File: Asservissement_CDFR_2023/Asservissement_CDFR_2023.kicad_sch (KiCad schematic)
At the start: 21 parts

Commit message: add one driver a3930
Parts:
- added C10, C11, C12: 47nF, symbol Device:C_Small
- added C13, C9: 1uF, symbol Device:C
- added C14: 220uF, symbol Device:C_Polarized
- added C7: 100nf, symbol Device:C
- added C8: 470nF, symbol Device:C
- added CT1: 470pF, symbol Device:C
- added IC1: A3930KJPTR-T, A3930KJPTR-T:A3930KJPTRT, symbol A3930:A3930KJPTR-T
- added J4: Conn_01x05, symbol Connector_Generic:Conn_01x05
- added J5: Conn_01x03, symbol Connector_Generic:Conn_01x03
- added Q1, Q2, Q3, Q4, Q5, Q6: QM6006D, Package_TO_SOT_SMD:TO-252-2, symbol Transistor_FET:QM6006D
- added R10: 0.056, symbol Device:R
- added R11, R12, R13, R14, R8, R9: 560, symbol Device:R
- added R4, RT1: 56k, symbol Device:R
- added R5: 100k, symbol Device:R
- added R6, R7: R, symbol Device:R
- gave numbers to parts that had none: 21
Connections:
- net +5V: now also J4.5 (Pin_5), R5.2, R6.1
- net +BATT: now also C13.1, C14.1, C7.1, IC1.24 (VDRAIN_), IC1.45 (VBB), Q1.2 (D), Q3.2 (D), Q5.2 (D)
- net -BATT renamed GND
- net GND: now also C13.2, C14.2, C7.2, C9.1, CT1.2, IC1.17 (TEST_), IC1.21 (CSN_), IC1.41 (AGND_1), IC1.49 (AGND_2), J4.1 (Pin_1), R10.2, R4.2, R7.2, RT1.2
- new net: IC1.20 (REF_), R5.1
- new net: IC1.29 (GHB), R12.1
- new net: Q4.1 (G), R12.2
- new net: Q3.1 (G), R11.2
- new net: C11.2, IC1.28 (SB), J5.2 (Pin_2), Q3.3 (S), Q4.2 (D)
- new net: Q5.1 (G), R13.2
- new net: C10.2, IC1.31 (SA), J5.3 (Pin_3), Q5.3 (S), Q6.2 (D)
- new net: CT1.1, IC1.16 (RC_), RT1.1
- new net: IC1.36 (GLA), R13.1
- new net: C11.1, IC1.30 (CB)
- new net: IC1.10 (H1_), J4.4 (Pin_4)
- new net: IC1.11 (H2_), J4.3 (Pin_3)
- new net: IC1.12 (H3_), J4.2 (Pin_2)
- new net: IC1.18 (RDEAD_), R4.1
- new net: IC1.22 (CSP_), IC1.38 (LSS), Q2.3 (S), Q4.3 (S), Q6.3 (S), R10.1
- new net: IC1.23 (VDSTH_), R6.2, R7.1
- new net: C12.2, IC1.25 (SC), J5.1 (Pin_1), Q1.3 (S), Q2.2 (D)
- new net: IC1.26 (GHC), R9.1
- new net: C12.1, IC1.27 (CC)
- new net: IC1.32 (GHA), R14.1
- new net: C10.1, IC1.33 (CA)
- new net: IC1.34 (GLC), R8.1
- new net: IC1.35 (GLB), R11.1
- new net: C9.2, IC1.40 (VREG)
- new net: C8.2, IC1.42 (CP1)
- new net: C8.1, IC1.43 (CP2)
- new net: Q1.1 (G), R8.2
- new net: Q6.1 (G), R14.2
- new net: Q2.1 (G), R9.2
- new net MODE_1: IC1.15 (MODE_)
- new net action_fault: IC1.39 (ESF)
- new net dir_info_1: IC1.44 (DIRO)
- new net direction_controle_1: IC1.9 (DIR_)
- new net disable_1: IC1.46 (COAST)
- new net erreur_1_1: IC1.5 (FF2_)
- new net erreur_2_1: IC1.6 (FF1_)
- new net frein_1: IC1.8 (BRAKE_)
- new net reset_1: IC1.2 (RESET_)
- new net speed_controle_1: IC1.14 (PWM_)
- new net vitesse_1: IC1.7 (TACHO_)
- no-connect marks 0 -> 8
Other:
- note added: "Blank time 650ns"
- note added: "CBOOT = QGATE × 20 / VBOOT Vboot = Vreg"
- note added: "Cesf 20 times larger than the bootstrap capacitor"
- note added: "ID max = 35A => Vds = 0.5V VDSTH = 0.5V"
- note added: "ITRIP = (VREF - VOOS) / (RSENSE×AV) Av = 19 Voos = 0.32V Vref = 4V max (limité) Itrip = courant max"
- note added: "Piste indépendant faible impédance pour lss"
- note added: "Vdrain : close to the drain connections of the high-side FETs, with an independent trace"
- note added: "tBLANK (µs) = 1260× CT (µF) fOSC ≈ 1/(RTCT + tBLANK + tDEAD) fOSC < fPWM"
- moved on the sheet: J1

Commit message: driver set up
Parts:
- removed IC1: A3930KJPTR-T, A3930KJPTR-T:A3930KJPTRT, symbol A3930:A3930KJPTR-T
- removed U1, U2: LM317_TO-263, Package_TO_SOT_SMD:TO-263-2, symbol Regulator_Linear:LM317_TO-263
- added C? (x3): 47nF, Capacitor_SMD:C_0805_2012Metric_Pad1.18x1.45mm_HandSolder, symbol Device:C_Small
- added C?: 100nF, Capacitor_SMD:C_0805_2012Metric_Pad1.18x1.45mm_HandSolder, symbol Device:C
- added C? (x2): 10uF, Capacitor_SMD:C_0805_2012Metric_Pad1.18x1.45mm_HandSolder, symbol Device:C
- added C? (x2): 1uF, Capacitor_SMD:C_0805_2012Metric_Pad1.18x1.45mm_HandSolder, symbol Device:C
- added C?: 220uF, symbol Device:C_Polarized
- added C?: 470nF, Capacitor_SMD:C_0805_2012Metric_Pad1.18x1.45mm_HandSolder, symbol Device:C
- added CT?: 470pF, Capacitor_SMD:C_0805_2012Metric_Pad1.18x1.45mm_HandSolder, symbol Device:C
- added IC? (x2): A3930KJPTR-T, A3930KJPTR-T:A3930KJPTRT, symbol a3930kjptr-t:A3930KJPTR-T
- added J?: Conn_01x05, symbol Connector_Generic:Conn_01x05
- added J? (x3): Conn_01x03, symbol Connector_Generic:Conn_01x03
- added JP?: Jumper_3_Open, symbol Jumper:Jumper_3_Open
- added Q? (x6): QM6006D, Package_TO_SOT_SMD:TO-252-2, symbol Transistor_FET:QM6006D
- added R15, R16, R17, R? (x5): R, Resistor_SMD:R_0805_2012Metric_Pad1.20x1.40mm_HandSolder, symbol Device:R
- added R? (x6): 560, Resistor_SMD:R_0805_2012Metric_Pad1.20x1.40mm_HandSolder, symbol Device:R
- added R?: 0.018, Resistor_SMD:R_2512_6332Metric, symbol Device:R
- added R?, RT?: 56k, Resistor_SMD:R_0805_2012Metric_Pad1.20x1.40mm_HandSolder, symbol Device:R
- added R?: 10k, symbol Device:R
- added R?: 100k, Resistor_SMD:R_0805_2012Metric_Pad1.20x1.40mm_HandSolder, symbol Device:R
- added U1, U2: LM317_SOT-223, Package_TO_SOT_SMD:SOT-223-3_TabPin2, symbol Regulator_Linear:LM317_SOT-223
- C10, C11, C12, C13, C8, C9, CT1: footprint (none) -> Capacitor_SMD:C_0805_2012Metric_Pad1.18x1.45mm_HandSolder
- C7: value 100nf -> 100nF; footprint (none) -> Capacitor_SMD:C_0805_2012Metric_Pad1.18x1.45mm_HandSolder
- R10: value 0.056 -> 0.018; footprint (none) -> Resistor_SMD:R_2512_6332Metric; Imax pour 3.4A max -> pour 10.7A max
- R11, R12, R13, R14, R4, R5, R6, R7, R8, R9, RT1: footprint (none) -> Resistor_SMD:R_0805_2012Metric_Pad1.20x1.40mm_HandSolder
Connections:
- net +3.3V: now also JP?.3 (B), U2.2 (VO)
- net +5V: now also J?.5 (Pin_5), R15.1, R16.1, R17.1, R?.1, R?.1, R?.1, R?.1, R?.2, U1.2 (VO)
- net +BATT: now also C?.1, C?.1, C?.1, C?.1, C?.1, IC?.24 (VDRAIN_), IC?.24 (VDRAIN_), IC?.45 (VBB), IC?.45 (VBB), Q?.2 (D), Q?.2 (D), Q?.2 (D)
- net GND: now also C?.1, C?.2, C?.2, C?.2, C?.2, C?.2, CT?.2, IC?.17 (TEST_), IC?.17 (TEST_), IC?.21 (CSN_), IC?.21 (CSN_), IC?.41 (AGND_1), IC?.41 (AGND_1), IC?.49 (AGND_2), IC?.49 (AGND_2), J?.1 (Pin_1), J?.3 (Pin_3), J?.3 (Pin_3), JP?.1 (A), R?.2, R?.2, R?.2, RT?.2
- net MODE_1: now also IC?.15 (MODE_), IC?.15 (MODE_)
- net action_fault: now also IC?.39 (ESF), IC?.39 (ESF)
- net dir_info_1: now also IC?.44 (DIRO), IC?.44 (DIRO)
- net direction_controle_1: now also IC?.9 (DIR_), IC?.9 (DIR_)
- net disable_1: now also IC?.46 (COAST), IC?.46 (COAST)
- net erreur_1_1: now also IC?.5 (FF2_), IC?.5 (FF2_)
- net erreur_2_1: now also IC?.6 (FF1_), IC?.6 (FF1_)
- net frein_1: now also IC?.8 (BRAKE_), IC?.8 (BRAKE_)
- net reset_1: now also IC?.2 (RESET_), IC?.2 (RESET_)
- net speed_controle_1: now also IC?.14 (PWM_), IC?.14 (PWM_)
- net vitesse_1: now also IC?.7 (TACHO_), IC?.7 (TACHO_)
- net at R5.1: now also IC?.20 (REF_)
- net SWCLK: now reaches J2.2 (Pin_2)
- net SWCLK: now also U3.49 (PA14)
- net SWDIO: now reaches J2.3 (Pin_3)
- net SWDIO: now also U3.46 (PA13)
- net at RV1.2: now also U1.1 (ADJ)
- net at C1.1, C2.1, M1.3 (S)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: now also U1.3 (VI), U2.3 (VI)
- net at R12.1: now also IC?.35 (GLB)
- net TX: now reaches U3.16 (PA2)
- net TX: now also J?.1 (Pin_1)
- net RX: now reaches U3.17 (PA3)
- net RX: now also J?.2 (Pin_2)
- net I2C_CLK: now reaches U3.58 (PB6)
- net I2C_CLK: now also J?.1 (Pin_1)
- net I2C_SDA: now reaches U3.59 (PB7)
- net I2C_SDA: now also J?.2 (Pin_2)
- net at U3.60 (BOOT0): now also R?.2
- net at C11.2, J5.2 (Pin_2), Q3.3 (S)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: now also IC?.28 (SB)
- net at C10.2, J5.3 (Pin_3), Q5.3 (S)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: now also IC?.31 (SA)
- net at CT1.1, RT1.1: now also IC?.16 (RC_)
- net at R13.1: now also IC?.32 (GHA)
- net at RV2.2: now also U2.1 (ADJ)
- net at C11.1: now also IC?.30 (CB)
- net at J4.4 (Pin_4): now also IC?.10 (H1_), R15.2
- net at J4.3 (Pin_3): now also IC?.11 (H2_), R16.2
- net at J4.2 (Pin_2): now also IC?.12 (H3_), R17.2
- net at R4.1: now also IC?.18 (RDEAD_)
- net at Q2.3 (S), Q4.3 (S), Q6.3 (S)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: now also IC?.22 (CSP_), IC?.38 (LSS)
- net at R6.2, R7.1: now also IC?.23 (VDSTH_)
- net at C12.2, J5.1 (Pin_1), Q1.3 (S)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: now also IC?.25 (SC)
- net at R9.1: now also IC?.34 (GLC)
- net at C12.1: now also IC?.27 (CC)
- net at R14.1: now also IC?.36 (GLA)
- net at C10.1: now also IC?.33 (CA)
- net at R8.1: now also IC?.26 (GHC)
- net at R11.1: now also IC?.29 (GHB)
- net at C9.2: now also IC?.40 (VREG)
- net at C8.2: now also IC?.42 (CP1)
- net at C8.1: now also IC?.43 (CP2)
- new net: C?.1, IC?.33 (CA)
- new net: C?.2, IC?.31 (SA), J?.3 (Pin_3), Q?.2 (D), Q?.3 (S)
- new net: Q?.1 (G), R?.2 (x6)
- new net: C?.2, IC?.25 (SC), J?.1 (Pin_1), Q?.2 (D), Q?.3 (S)
- new net: IC?.10 (H1_), J?.4 (Pin_4), R?.2
- new net: IC?.36 (GLA), R?.1
- new net: IC?.34 (GLC), R?.1
- new net: IC?.22 (CSP_), IC?.38 (LSS), Q?.3 (S), Q?.3 (S), Q?.3 (S), R?.1
- new net: IC?.29 (GHB), R?.1
- new net: C?.2, IC?.40 (VREG)
- new net: IC?.26 (GHC), R?.1
- new net: IC?.23 (VDSTH_), R?.1, R?.2
- new net: IC?.18 (RDEAD_), R?.1
- new net: IC?.12 (H3_), J?.2 (Pin_2), R?.2
- new net: IC?.11 (H2_), J?.3 (Pin_3), R?.2
- new net: C?.2, IC?.28 (SB), J?.2 (Pin_2), Q?.2 (D), Q?.3 (S)
- new net: CT?.1, IC?.16 (RC_), RT?.1
- new net: JP?.2 (C), R?.1
- new net: IC?.35 (GLB), R?.1
- new net: C?.1, IC?.30 (CB)
- new net: C?.1, IC?.27 (CC)
- new net: C?.1, IC?.43 (CP2)
- new net: C?.2, IC?.42 (CP1)
- new net: IC?.20 (REF_), R?.1
- new net: IC?.32 (GHA), R?.1
- new net Info_Courant_1: IC?.19 (CSOUT_), IC?.19 (CSOUT_)
- no-connect marks 8 -> 14
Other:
- moved on the sheet: C5, C6, C7, CT1, J2, J3, R4, R5, RT1, U3, Y1

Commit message: Maj de l'alimenter ok reste microcontrol
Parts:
- removed RV1, RV2: R_Potentiometer, symbol Device:R_Potentiometer
- added R10: 710, symbol Device:R
- added R2, R8: 240, symbol Device:R
- added R4: 390, symbol Device:R
- R3: value R -> 25
- R9: renamed from R2; value R -> 150
- gave numbers to parts that had none: 40
- renumbered C8 to C1, C1 to C10, C3 to C11, C11 to C12, C12 to C13, C5 to C14, C6 to C15, C7 to C3, C9 to C4, C13 to C5, C14 to C6, C2 to C7, C4 to C8, C10 to C9, D2 to D1, D1 to D2, J5 to J2, J4 to J3, J2 to J4, J3 to J6, Q3 to Q2, Q5 to Q3, Q2 to Q4, Q4 to Q5, R15 to R11, R16 to R12, R17 to R13, R9 to R14, R12 to R15, R14 to R16, R10 to R17, R4 to R18, R5 to R19, R6 to R20, R7 to R22, R8 to R5, R11 to R6, R13 to R7, U2 to U1, U1 to U2
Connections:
- net +3.3V: now also R2.1
- net +5V: now also R8.1
- net GND: now also R10.2, R4.2
- net at U1.1 (ADJ): now also R2.2, R4.1
- net at U2.1 (ADJ): now also R10.1, R8.2

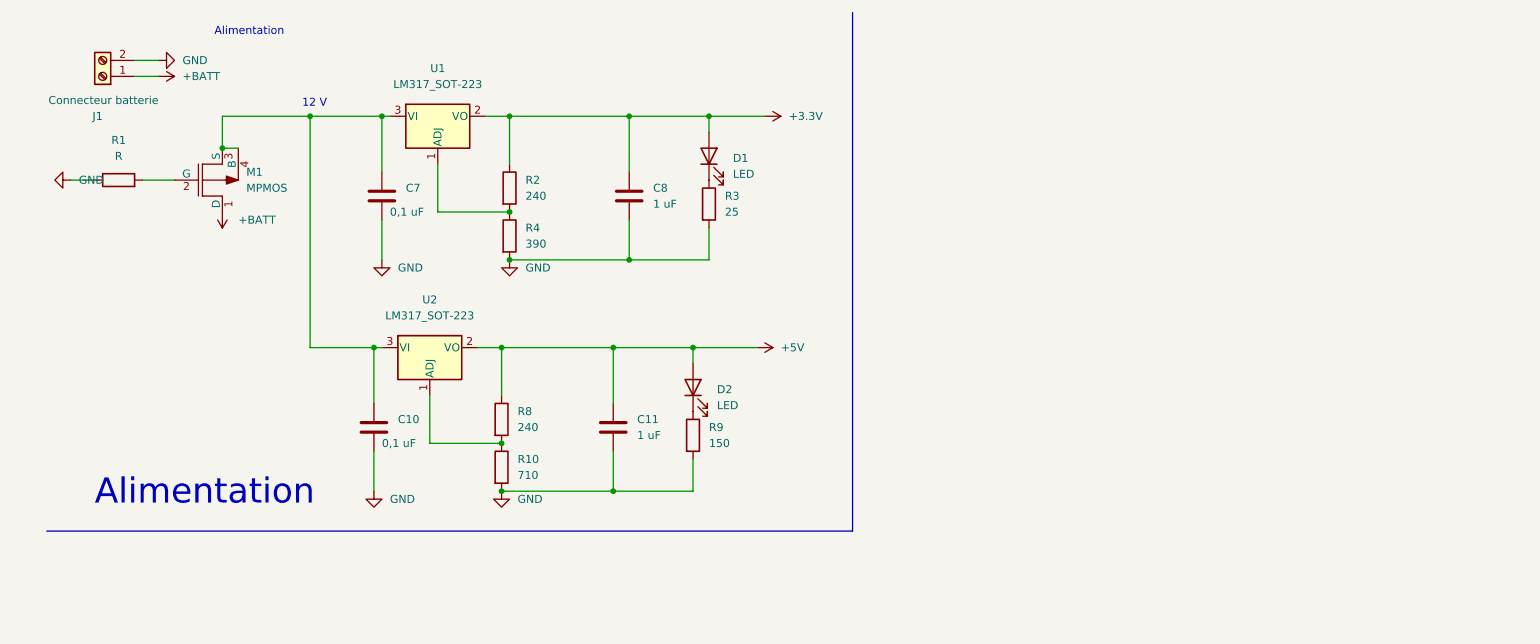
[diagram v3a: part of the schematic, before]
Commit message: Buck converter, fix gitignore
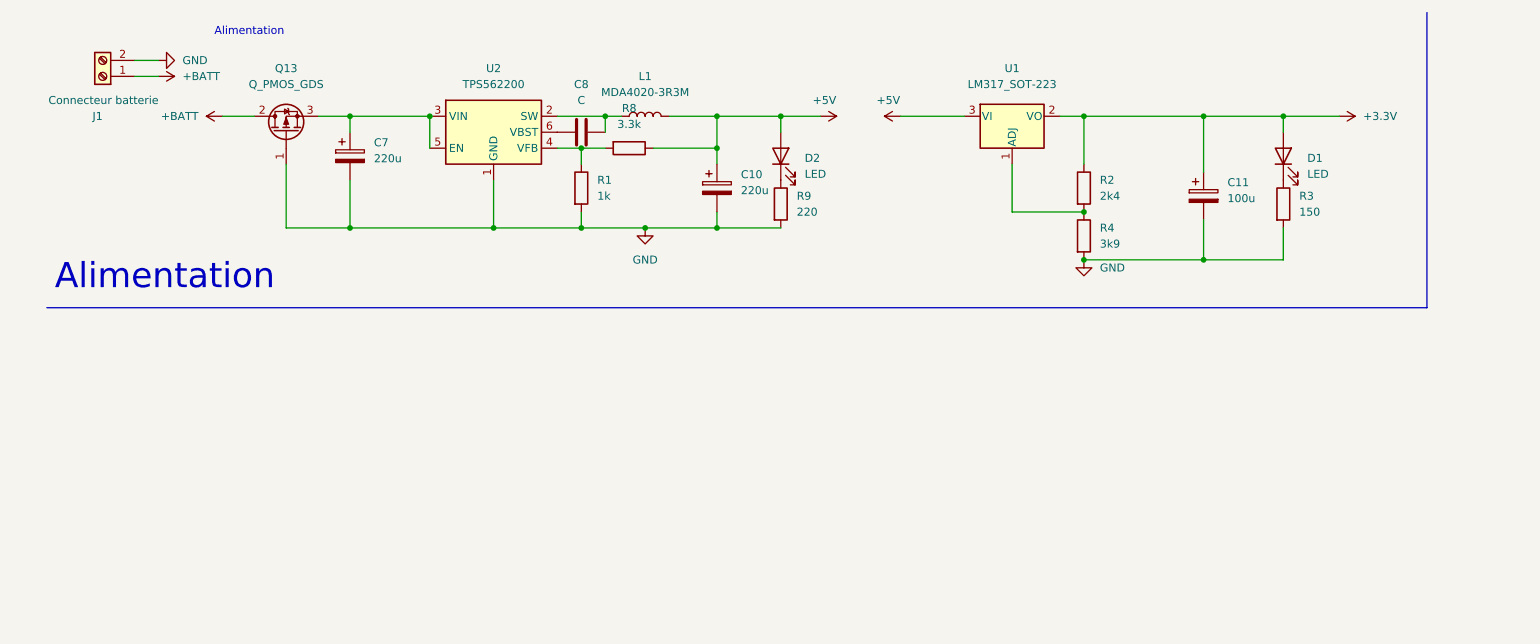
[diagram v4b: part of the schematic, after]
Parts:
- removed C10, C7: 0,1 uF, Capacitor_SMD:C_0805_2012Metric_Pad1.18x1.45mm_HandSolder, symbol Device:C
- removed C11: 1 uF, Capacitor_SMD:C_0805_2012Metric_Pad1.18x1.45mm_HandSolder, symbol Device:C
- removed M1: MPMOS, symbol pspice:MPMOS
- removed R10: 710, symbol Device:R
- removed U2: LM317_SOT-223, Package_TO_SOT_SMD:SOT-223-3_TabPin2, symbol Regulator_Linear:LM317_SOT-223
- added C10: 220u, Capacitor_THT:CP_Radial_D8.0mm_P5.00mm, symbol Device:C_Polarized
- added C11: 100u, Capacitor_THT:CP_Radial_D8.0mm_P3.80mm, symbol Device:C_Polarized
- added C7: 220u, Capacitor_THT:CP_Radial_D10.0mm_P5.00mm, symbol Device:C_Polarized
- added L1: MDA4020-3R3M, Inductor_SMD:L_Vishay_IFSC-1515AH_4x4x1.8mm, symbol Device:L
- added Q13: Q_PMOS_GDS, symbol Device:Q_PMOS_GDS
- added U2: TPS562200, Package_TO_SOT_SMD:SOT-23-6, symbol Regulator_Switching:TPS562200
- C8: value 1 uF -> C; footprint Capacitor_SMD:C_0805_2012Metric_Pad1.18x1.45mm_HandSolder -> (none)
- R1: value R -> 1k; footprint Resistor_SMD:R_0805_2012Metric_Pad1.20x1.40mm_HandSolder -> (none)
- R2: value 240 -> 2k4
- R3: value 25 -> 150
- R4: value 390 -> 3k9
- R8: value 240 -> 3.3k
- R9: value 150 -> 220
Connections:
- net +3.3V: now also C11.1; no longer C8.1
- net +5V: now also U1.3 (VI), C10.1, L1.2
- net +BATT: now also Q13.2 (D)
- net GND: now also R1.2, C10.2, C11.2, C7.2, Q13.1 (G), U2.1 (GND); no longer C8.2, R1.1
- net at R8.2: now also R1.1, U2.4 (VFB)
- new net: C8.2, L1.1, U2.2 (SW)
- new net: C7.1, Q13.3 (S), U2.3 (VIN), U2.5 (EN)
- new net: C8.1, U2.6 (VBST)
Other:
- note removed: "12 V"
- moved on the sheet: D1, D2, R2, R3, R4, R9, U1

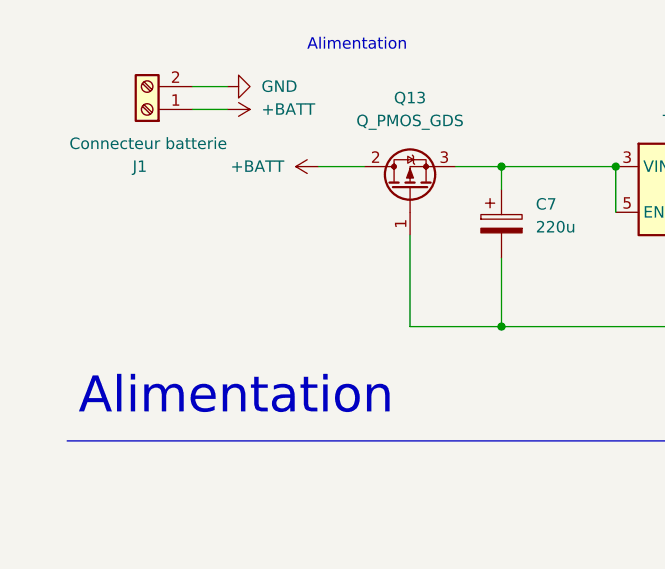
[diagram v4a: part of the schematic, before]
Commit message: NMOS reverse voltage protection
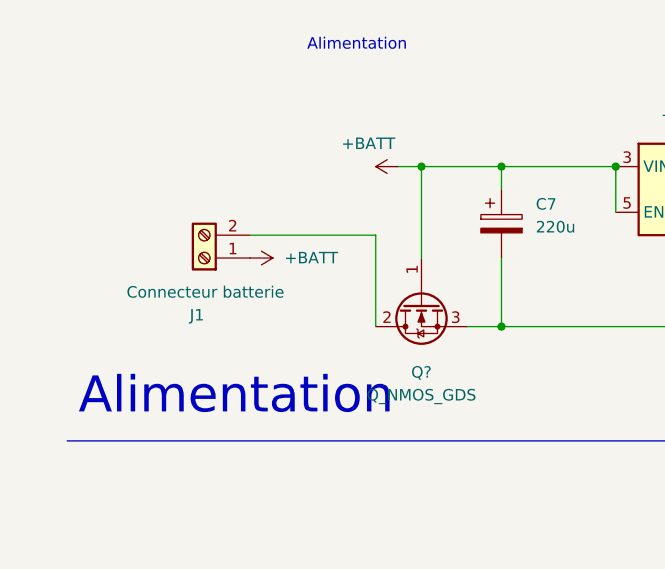
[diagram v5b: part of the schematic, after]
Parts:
- removed Q13: Q_PMOS_GDS, symbol Device:Q_PMOS_GDS
- added Q?: Q_NMOS_GDS, symbol Device:Q_NMOS_GDS
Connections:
- net +BATT: now also C7.1, U2.3 (VIN), U2.5 (EN), Q?.1 (G)
- net GND: now also Q?.3 (S); no longer J1.2 (Pin_2)
- new net: J1.2 (Pin_2), Q?.2 (D)
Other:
- moved on the sheet: J1
